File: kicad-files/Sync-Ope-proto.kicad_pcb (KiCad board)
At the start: 2 copper layers, 100 x 100 mm, 51 parts, among them J1 VIDEO_INPUT, J2 euro_power, J3 VIDEO_SEND, J4 VIDEO_RETURN, J5 CV_IN, J6 VIDEO_OUTPUT, U1 AD8072, U2 LM1881, U3 L7805, U4 L7905, U5 LT1251, U6 CD4053BE

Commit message: updating schematic and pcb for 0.1proto
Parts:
- added C12: 200u, Capacitor_THT:CP_Radial_D5.0mm_P2.50mm, F.Cu at (153.5, 71.0)
- added C13: 200u, Capacitor_THT:CP_Radial_D5.0mm_P2.50mm, F.Cu at (147.0, 71.0)
- added D4: 1n4007, Diode_THT:D_DO-35_SOD27_P7.62mm_Horizontal, F.Cu at (159.0, 66.5)
- added D5: 1n4007, Diode_THT:D_DO-35_SOD27_P7.62mm_Horizontal, F.Cu at (148.5, 66.5)
- added D6: zener_1.8v, Diode_THT:D_DO-35_SOD27_P7.62mm_Horizontal, F.Cu at (180.5, 133.5)
- added D7: schottky, Diode_THT:D_DO-35_SOD27_P7.62mm_Horizontal, F.Cu at (180.5, 137.0)
- added J7: AC_POWER, Connector_BarrelJack:BarrelJack_Horizontal, F.Cu at (149.5, 60.0)
- added J8: diy_power_header, Connector_PinHeader_2.54mm:PinHeader_1x03_P2.54mm_Vertical, F.Cu at (196.5, 95.0)
- R12: value 100k -> 470k
- R13: value 100 -> 75
- R3: value 100 -> 220
- moved R3 68.3 mm to (146.5, 128.5)
- moved C2 14.5 mm to (166.5, 56.0)
- moved R10 14.5 mm to (164.5, 53.0)
- moved R7 14.5 mm to (161.5, 53.0)
- moved R20 0.71 mm to (174.5, 52.0)
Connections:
- C3 pad 2: Net-(C3-Pad2) -> VIDEO_TO_SYNC
- R3 pad 1: Net-(C3-Pad2) -> Net-(J5-PadT)
- R3 pad 2: VIDEO_TO_SYNC -> Net-(R3-Pad2)
- U6 pad 3: Net-(J5-PadT) -> Net-(R3-Pad2)
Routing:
- net -12V: track 18.6 -> 95.6 mm
- net +12V: track 33.5 -> 100.0 mm
- net +5V: track 94.2 -> 50.8 mm
- net Net-(J5-PadT): track 44.3 -> 7.30 mm
- net Net-(R3-Pad2): track 0.00 -> 35.0 mm
- net GND: track 69.1 -> 36.3 mm, vias 2 -> 1
- net Net-(R2-Pad1): track 30.2 -> 44.1 mm
- net Net-(D4-Pad2): track 0.00 -> 9.79 mm
- net Net-(D6-Pad1): track 106.4 -> 113.8 mm
- net VIDEO_TO_SYNC: track 23.8 -> 30.2 mm
- net -5V: track 148.9 -> 142.8 mm
- net Net-(C3-Pad2): track 5.62 -> 0.00 mm
- net Net-(R15-Pad2): track 55.8 -> 53.2 mm
- net DRY_BLANKED_SIGNAL: track 121.4 -> 119.9 mm
- net Net-(J6-Pad2): track 15.5 -> 14.8 mm

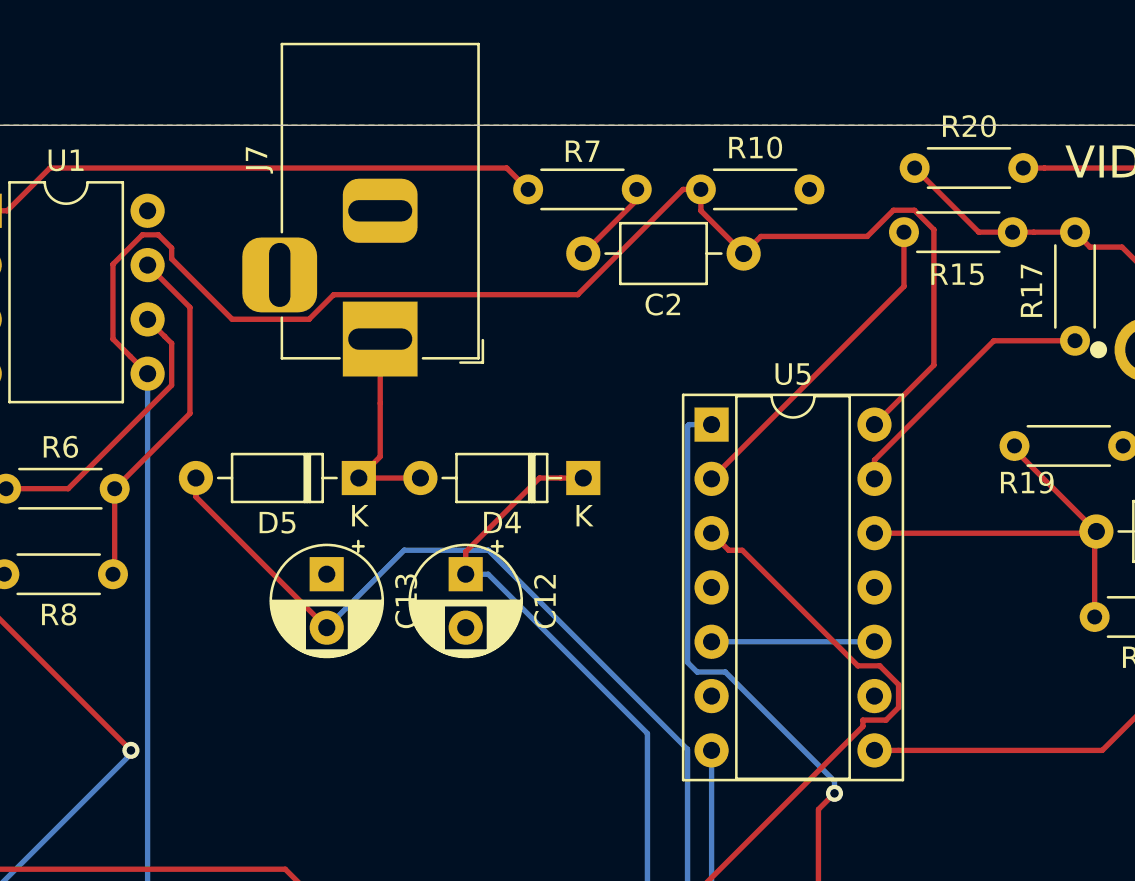
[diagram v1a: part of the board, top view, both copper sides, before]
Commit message: update a trace for proto0.1 order
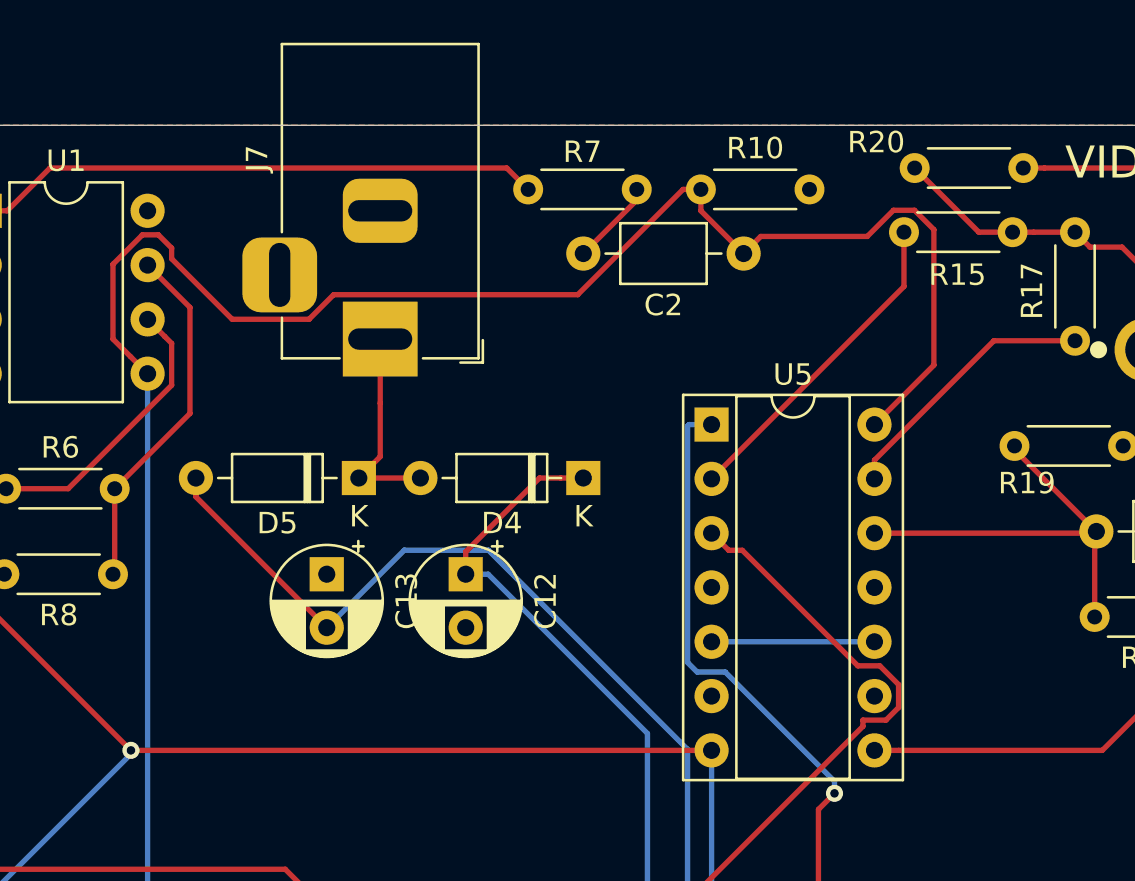
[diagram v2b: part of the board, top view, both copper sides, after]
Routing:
- net -5V: track 142.8 -> 170.0 mm
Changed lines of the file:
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@@
     (thickness 1.6)
     (drawings 10)
-    (tracks 271)
+    (tracks 272)
     (zones 0)
     (modules 59)
@@
     (descr "Resistor, Axial_DIN0204 series, Axial, Horizontal, pin pitch=5.08mm, 0.167W, length*diameter=3.6*1.6mm^2, http://cdn-reichelt.de/documents/datenblatt/B400/1_4W%23YAG.pdf")
     (tags "Resistor Axial_DIN0204 series Axial Horizontal pin pitch 5.08mm 0.167W length 3.6mm diameter 1.6mm")
-    (fp_text reference R20 (at 2.54 -1.92) (layer F.SilkS)
+    (fp_text reference R20 (at -1.8 -1.2) (layer F.SilkS)
       (effects (font (size 1 1) (thickness 0.15)))
     )
@@
   (segment (start 188.3 95) (end 196.5 95) (width 0.25) (layer F.Cu) (net 12))
   (segment (start 179.2 104.1) (end 188.3 95) (width 0.25) (layer F.Cu) (net 12))
+  (segment (start 137.84 79.24) (end 165 79.24) (width 0.25) (layer F.Cu) (net 12))
   (segment (start 153.05 86.6) (end 151.8 87.85) (width 0.25) (layer F.Cu) (net 13))
   (segment (start 151.8 87.85) (end 151.8 89) (width 0.25) (layer F.Cu) (net 13))

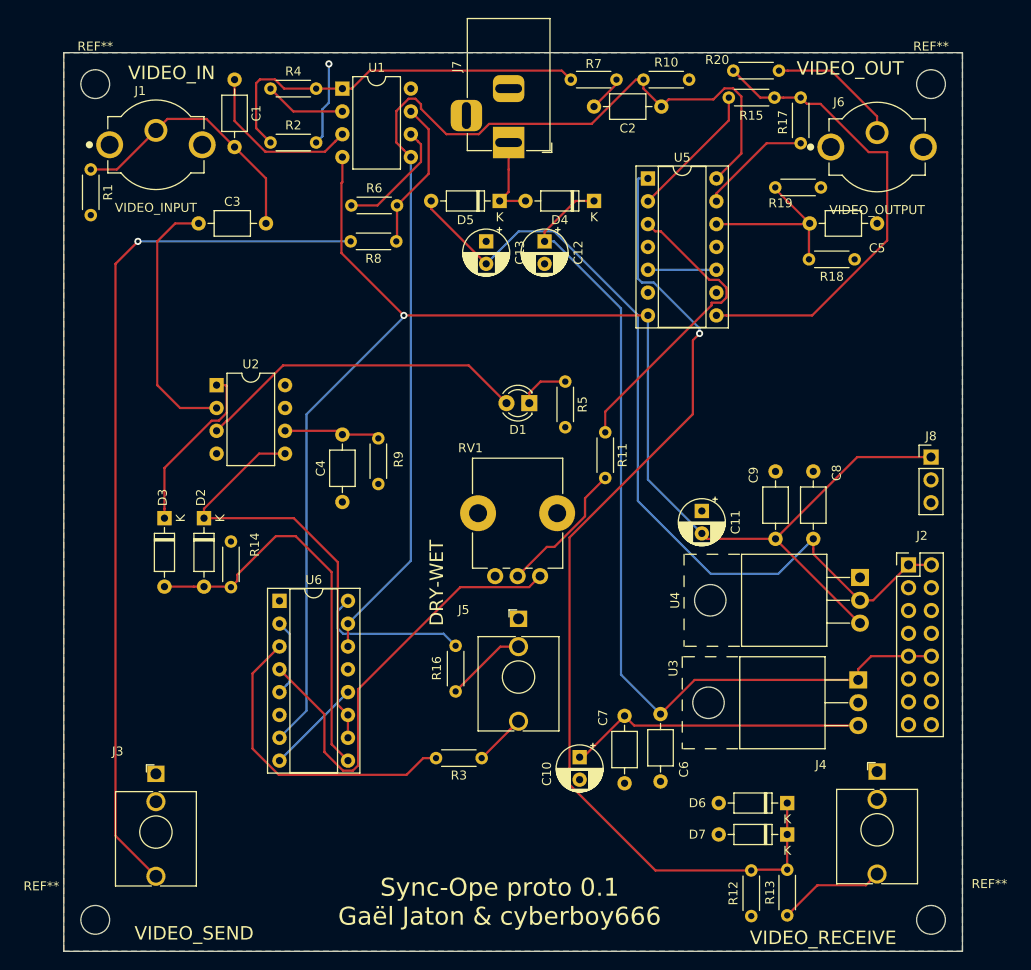
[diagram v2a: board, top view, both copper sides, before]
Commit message: update circuit design to 0.2
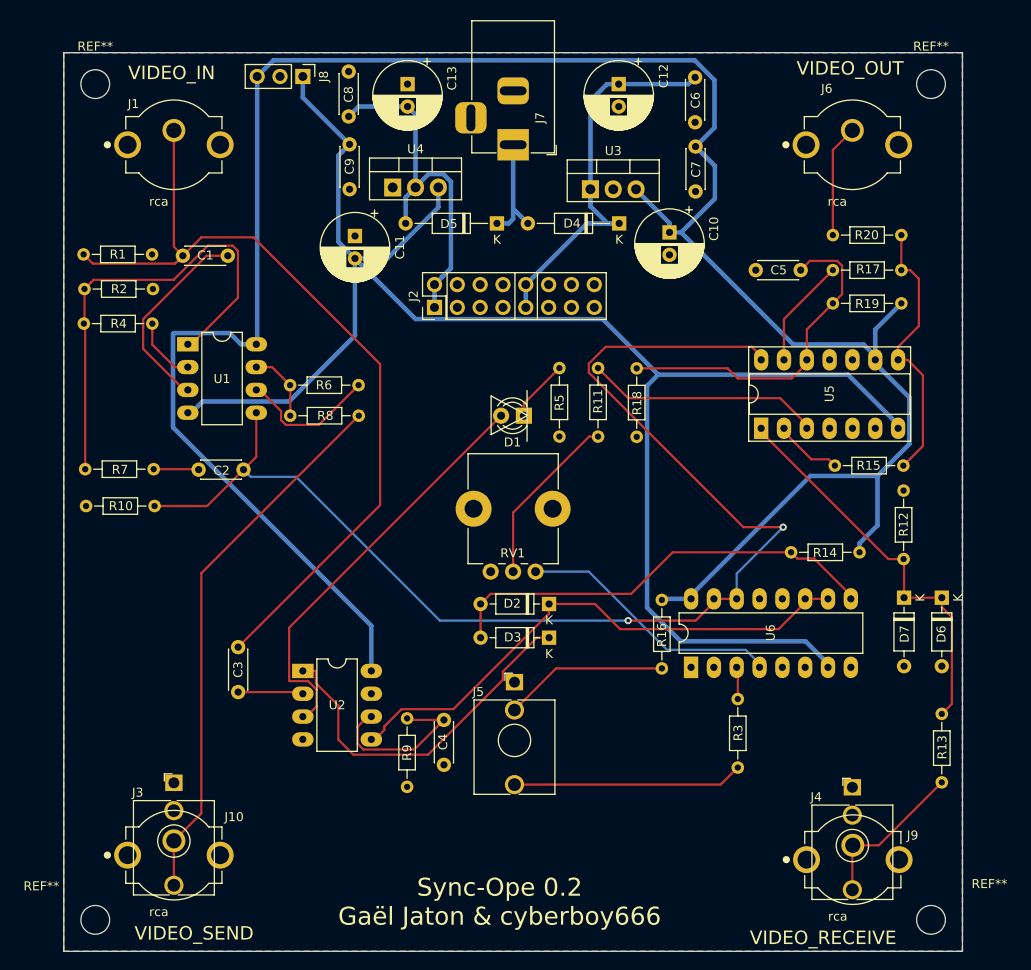
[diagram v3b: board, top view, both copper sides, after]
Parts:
- added J10: rca, lib_fp:RCJ-024, F.Cu at (112.2, 139.3)
- added J9: rca, lib_fp:RCJ-024, F.Cu at (187.8, 139.8)
- C1, C2, C3, C4, C5, C6, C7, C8, C9: footprint Capacitor_THT:C_Axial_L3.8mm_D2.6mm_P7.50mm_Horizontal -> Capacitor_THT:C_Disc_D4.3mm_W1.9mm_P5.00mm
- C10, C11, C12, C13: footprint Capacitor_THT:CP_Radial_D5.0mm_P2.50mm -> Capacitor_THT:CP_Radial_D7.5mm_P2.50mm
- D2, D3: value D -> 1n4148
- D4, D5: footprint Diode_THT:D_DO-35_SOD27_P7.62mm_Horizontal -> Diode_THT:D_DO-35_SOD27_P10.16mm_Horizontal
- J1: value VIDEO_INPUT -> rca; footprint project_parts:RCJ-024 -> lib_fp:RCJ-024
- J3: value VIDEO_SEND -> mono_jack
- J4: value VIDEO_RETURN -> mono_jack
- J5: value CV_IN -> mono_jack
- J6: value VIDEO_OUTPUT -> rca; footprint project_parts:RCJ-024 -> lib_fp:RCJ-024
- R1, R10, R11, R12, R13, R14, R15, R16, R17, R18, R19, R2, R20, R3, R4, R5, R6, R7, R8, R9: footprint Resistor_THT:R_Axial_DIN0204_L3.6mm_D1.6mm_P5.08mm_Horizontal -> Resistor_THT:R_Axial_DIN0204_L3.6mm_D1.6mm_P7.62mm_Horizontal
- U1, U2: footprint Package_DIP:DIP-8_W7.62mm -> Package_DIP:DIP-8_W7.62mm_LongPads
- U3, U4: footprint Package_TO_SOT_THT:TO-220-3_Horizontal_TabUp -> Package_TO_SOT_THT:TO-220-3_Vertical
- U5: footprint Package_DIP:DIP-14_W7.62mm_Socket -> Package_DIP:DIP-14_W7.62mm_Socket_LongPads
- U6: footprint Package_DIP:DIP-16_W7.62mm_Socket -> Package_DIP:DIP-16_W7.62mm_LongPads
- moved J8 81.7 mm to (126.6, 52.6), turned to 270 degrees
- moved R10 72.2 mm to (110.1, 100.5), turned to 180 degrees
- moved C6 71.0 mm to (170.2, 52.8)
- moved R14 70.0 mm to (188.6, 105.6), turned to 180 degrees
- moved C8 68.2 mm to (131.7, 52.1)
- moved U4 67.7 mm to (136.6, 65.0), turned to 0 degrees
- moved R7 67.3 mm to (110.0, 96.3)
- moved C7 63.8 mm to (170.3, 60.5)
- moved U3 62.2 mm to (158.6, 65.2), turned to 0 degrees
- moved C2 61.6 mm to (120.0, 96.4)
- moved J2 60.0 mm to (141.2, 78.3), turned to 90 degrees
- moved C10 59.2 mm to (167.4, 70.0)
- moved C9 56.9 mm to (131.8, 65.2), turned to 90 degrees
- moved C3 52.3 mm to (119.4, 121.2), turned to 90 degrees
- moved C11 49.3 mm to (132.4, 70.4)
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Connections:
- J1 pad 2: VIDEO_TO_SYNC -> GND
- J6 pad 2: Net-(J6-Pad2) -> GND
- J7 pad 3: (no net) -> Net-(J7-Pad3)
- R20 pad 2: Net-(J6-Pad2) -> Net-(J6-Pad1)
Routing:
- net +5V: track 50.8 -> 257.2 mm
- net Net-(D6-Pad1): track 113.8 -> 44.5 mm, vias 1 -> 0
- net VIDEO_TO_SYNC: track 30.2 -> 92.9 mm
- net +12V: track 100.0 -> 44.2 mm
- net -12V: track 95.6 -> 40.5 mm
- net Net-(J10-Pad1): track 97.2 -> 60.8 mm, vias 1 -> 0
- net GND: track 36.3 -> 0.00 mm, vias 1 -> 0
- net Net-(R3-Pad2): track 35.0 -> 3.58 mm
- net Net-(R15-Pad2): track 53.2 -> 30.7 mm
- net DRY_BLANKED_SIGNAL: track 119.9 -> 142.2 mm, vias 0 -> 2
- net Net-(C3-Pad1): track 29.1 -> 7.28 mm
- net VIDEO_SYNC: track 19.2 -> 40.2 mm
- net ADDED_SYNC: track 50.1 -> 29.6 mm
- net Net-(J5-PadT): track 7.30 -> 25.6 mm
- net Net-(C5-Pad1): track 20.0 -> 37.8 mm
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- added copper zone on B.Cu, net GND
- removed copper zone on B.Cu, net +5V
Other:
- board text added: "Sync-Ope 0.2 Gaël Jaton & cyberboy666"
- board text removed: "DRY-WET"
- board text removed: "Sync-Ope proto 0.1 Gaël Jaton & cyberboy666"

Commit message: latest revision
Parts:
- moved J4 18.4 mm to (169.4, 131.0)
- moved J3 17.8 mm to (130.0, 131.0)
- moved R3 8.36 mm to (170.5, 122.5), turned to 0 degrees
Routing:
- net Net-(J10-Pad1): track 60.8 -> 76.6 mm
- net Net-(J4-PadT): track 17.8 -> 33.0 mm
- net Net-(R3-Pad2): track 3.58 -> 5.61 mm
- net Net-(J5-PadT): track 25.6 -> 24.2 mm
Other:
- board text added: "+5v"
- board text added: "-5v"
- board text added: "GND"
- board text added: "Sync-Ope 0.2.1 Gaël Jaton & cyberboy666"
- board text removed: "Sync-Ope 0.2 Gaël Jaton & cyberboy666"

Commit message: circuit revision 0.3
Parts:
- removed D2, D3: 1n4148, Diode_THT:D_DO-35_SOD27_P7.62mm_Horizontal
- removed R10: 100k, Resistor_THT:R_Axial_DIN0204_L3.6mm_D1.6mm_P7.62mm_Horizontal
- removed the REF** at (103.5, 146.5)
- removed the REF** at (196.5, 146.5)
- removed the REF** at (196.5, 53.5)
- removed the REF** at (103.5, 53.5)
- added C14: 0.1u, Capacitor_THT:C_Disc_D4.3mm_W1.9mm_P5.00mm, F.Cu at (102.7, 93.8)
- added C15: 0.1u, Capacitor_THT:C_Disc_D4.3mm_W1.9mm_P5.00mm, F.Cu at (134.3, 121.3)
- added C16: 0.1u, Capacitor_THT:C_Disc_D4.3mm_W1.9mm_P5.00mm, F.Cu at (161.4, 139.3)
- added C17: 0.1u, Capacitor_THT:C_Disc_D4.3mm_W1.9mm_P5.00mm, F.Cu at (197.7, 84.1)
- added C18: 0.1u, Capacitor_THT:C_Disc_D4.3mm_W1.9mm_P5.00mm, F.Cu at (121.6, 93.4)
- added C19: 0.1u, Capacitor_THT:C_Disc_D4.3mm_W1.9mm_P5.00mm, F.Cu at (197.7, 86.8)
- added REF**: MountingHole_3.2mm_M3, MountingHole:MountingHole_3.2mm_M3, F.Cu at (196.6, 53.5)
- added REF**: MountingHole_3.2mm_M3, MountingHole:MountingHole_3.2mm_M3, F.Cu at (196.6, 146.5)
- added REF**: MountingHole_3.2mm_M3, MountingHole:MountingHole_3.2mm_M3, F.Cu at (103.5, 146.6)
- added REF**: MountingHole_3.2mm_M3, MountingHole:MountingHole_3.2mm_M3, F.Cu at (103.5, 53.5)
- added RV2: 5k_trim, lib_fp:tht_vertical_trim_3362, F.Cu at (157.2, 119.6)
- added U7: CD4053B, Package_DIP:DIP-16_W7.62mm_LongPads, F.Cu at (175.6, 101.6)
- C1: value 100n -> 0.001u; footprint Capacitor_THT:C_Disc_D4.3mm_W1.9mm_P5.00mm -> Capacitor_THT:C_Disc_D4.7mm_W2.5mm_P5.00mm
- C12, C13: value 200u -> 220u
- C2, C3, C4, C5, C7, C9: value 100n -> 0.1u
- C6, C8: value 330n -> 0.33u
- D1: value video signal indicator LED -> LED
- J1, J10, J6, J9: footprint lib_fp:RCJ-024 -> lib_fp:tht_vertical_rca
- J2: value euro_power -> europower
- J3, J4, J5: value mono_jack -> mono_jack_3.5mm
- J7: value AC_POWER -> barrel_jack
- R14: value 10k -> 680k
- R16: value 39k -> 1k
- R3: value 220 -> 510
- R5: value 1k -> 39k
- R9: value 680k -> 10k
- U1: footprint Package_DIP:DIP-8_W7.62mm_LongPads -> lib_fp:DIP-SOIC-8
- U2: value LM1881 -> 74HC4538; footprint Package_DIP:DIP-8_W7.62mm_LongPads -> Package_DIP:DIP-16_W7.62mm_LongPads
- U6: value CD4053BE -> LM1881; footprint Package_DIP:DIP-16_W7.62mm_LongPads -> lib_fp:DIP-SOIC-8
- moved J8 74.1 mm to (102.4, 122.7), turned to 180 degrees
- moved C1 70.6 mm to (162.2, 127.8)
- moved R14 54.2 mm to (134.4, 105.8), turned to 0 degrees
- moved R3 53.6 mm to (125.2, 93.8)
- moved C7 40.4 mm to (183.2, 98.7), turned to 180 degrees
- moved U6 35.6 mm to (134.3, 116.1), turned to 270 degrees
- moved U2 33.7 mm to (157.9, 131.3), turned to 270 degrees
- moved R5 30.9 mm to (164.7, 114.5), turned to 180 degrees
- moved R16 27.9 mm to (155.6, 85.2)
- moved C3 24.0 mm to (134.5, 102.5), turned to 0 degrees
- moved C4 21.5 mm to (134.5, 109.2), turned to 0 degrees
- moved R9 20.3 mm to (157.2, 124.5), turned to 0 degrees
- moved J5 8.75 mm to (149.9, 111.3)
- moved U1 8.17 mm to (119.8, 88.0), turned to 270 degrees
- moved D1 0.22 mm to (151.3, 90.6)
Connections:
- C1 pad 2: VIDEO_TO_SYNC -> Net-(C1-Pad2)
- C2 pad 1: DRY_BLANKED_SIGNAL -> /blanking/input_blank
- C3 pad 2: VIDEO_TO_SYNC -> /blanking/video_in
- C4 pad 1: GND -> Net-(C4-Pad1)
- C4 pad 2: Net-(C4-Pad2) -> GND
- J1 pad 1: VIDEO_TO_SYNC -> /blanking/video_in
- J3 pad TN: GND -> Net-(J3-PadTN)
- J4 pad T: Net-(J4-PadT) -> /blanking/return_blank
- J4 pad TN: GND -> Net-(J4-PadTN)
- J5 pad T: Net-(J5-PadT) -> /blanking/control_blank
- J9 pad 1: Net-(J4-PadT) -> /blanking/return_blank
- R1 pad 1: VIDEO_TO_SYNC -> /blanking/video_in
- R12 pad 1: Net-(D6-Pad1) -> GND
- R12 pad 2: GND -> Net-(D6-Pad1)
- R13 pad 1: Net-(J4-PadT) -> Net-(D6-Pad1)
- R13 pad 2: Net-(D6-Pad1) -> /blanking/return_blank
- R14 pad 1: +5V -> Net-(C4-Pad1)
- R14 pad 2: Net-(D2-Pad2) -> GND
- R16 pad 1: +5V -> Net-(D1-Pad1)
- R16 pad 2: Net-(J5-PadTN) -> GND
- R3 pad 1: Net-(J5-PadT) -> Net-(R3-Pad1)
- R3 pad 2: Net-(R3-Pad2) -> /blanking/video_in
- R5 pad 1: Net-(D1-Pad1) -> +5V
- R5 pad 2: GND -> Net-(J5-PadTN)
- R7 pad 2: Net-(R2-Pad1) -> Net-(R4-Pad1)
- R9 pad 1: GND -> Net-(C1-Pad2)
- R9 pad 2: Net-(C4-Pad2) -> Net-(R9-Pad2)
- RV1 pad 1: ADDED_SYNC -> /blanking/control_pulse
- U1 pad 1: Net-(R2-Pad1) -> Net-(R4-Pad1)
- U1 pad 2: Net-(R4-Pad1) -> Net-(R2-Pad1)
- U1 pad 3: Net-(C1-Pad1) -> Net-(R3-Pad1)
- U1 pad 5: DRY_BLANKED_SIGNAL -> /blanking/input_blank
- U2 pad 1: VIDEO_SYNC -> Net-(C1-Pad1)
- U2 pad 2: Net-(C3-Pad1) -> Net-(C1-Pad2)
- U2 pad 3: Net-(D1-Pad2) -> +5V
- U2 pad 5: BURST_SYNC -> Net-(U2-Pad5)
- U2 pad 6: Net-(C4-Pad2) -> Net-(U2-Pad6)
- U2 pad 8: +5V -> GND
- U5 pad 14: DRY_BLANKED_SIGNAL -> /blanking/input_blank
- U6 pad 1: Net-(U6-Pad1) -> Net-(U2-Pad5)
- U6 pad 2: GND -> Net-(C3-Pad1)
- U6 pad 3: Net-(R3-Pad2) -> Net-(D1-Pad2)
- U6 pad 4: ADDED_SYNC -> GND
- U6 pad 5: GND -> Net-(U6-Pad5)
- U6 pad 6: GND -> Net-(C4-Pad1)
- U6 pad 7: -5V -> Net-(U6-Pad7)
- U6 pad 8: GND -> +5V
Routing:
- net /blanking/input_blank: track 0.00 -> 166.9 mm, vias 0 -> 1
- net DRY_BLANKED_SIGNAL: track 142.2 -> 0.00 mm, vias 2 -> 0
- net VIDEO_TO_SYNC: track 92.9 -> 0.00 mm
- net /blanking/video_in: track 0.00 -> 76.4 mm
- net /blanking/return_blank: track 0.00 -> 64.3 mm
- net BURST_SYNC: track 60.7 -> 0.00 mm
- net Net-(R4-Pad1): track 7.33 -> 59.9 mm
- net Net-(U2-Pad5): track 0.00 -> 52.3 mm, vias 0 -> 1
- net Net-(D2-Pad2): track 49.7 -> 0.00 mm
- net Net-(U2-Pad6): track 0.00 -> 49.6 mm
- net -5V: track 186.7 -> 230.3 mm
- net /blanking/control_blank: track 0.00 -> 42.4 mm
- net VIDEO_SYNC: track 40.2 -> 0.00 mm
- net Net-(R3-Pad1): track 0.00 -> 39.2 mm
- net Net-(J4-PadT): track 33.0 -> 0.00 mm
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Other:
- board text added: "->"
- board text added: "12-15V AC"
- board text added: "CV_IN"
- board text added: "VIDEO_RETURN"
- board text added: "WET_DRY"
- board text added: "_^ 04"
- board text added: "sync_ope 0_3_0 Gaël Jaton & cyberboy666"
- board text added: "underscores.shop"
- board text removed: "Sync-Ope 0.2.1 Gaël Jaton & cyberboy666"
- board text removed: "VIDEO_RECEIVE"
